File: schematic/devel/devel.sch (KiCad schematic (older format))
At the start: 65 parts, among them J1 CONN_PWR, J2 CONN_X1, J3 CONN_Y2, J4 CONN_X2, J5 CONN_Y1, Q1 Q_PMOS_GSD, Q2 Q_NMOS_GSD, U1 LM317_SOT223, U2 LM337_SOT223, U3 REF5010IDGK, U4 OPA4197

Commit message: completed pcb layout routing
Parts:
- removed C17, C18: 100u, Capacitor_SMD:CP_Elec_4x3.9, symbol Device:CP_Small
- removed D4, D5: D_Zener_Small, Diode_SMD:D_0805_2012Metric, symbol Device:D_Zener_Small
- removed D8, D9: D_Small, Diode_SMD:D_0805_2012Metric, symbol Device:D_Small
- removed Q1: Q_PMOS_GSD, Package_TO_SOT_SMD:SOT-23, symbol Device:Q_PMOS_GSD
- removed Q2: Q_NMOS_GSD, Package_TO_SOT_SMD:SOT-23, symbol Device:Q_NMOS_GSD
- removed R10, R11: 100k, Resistor_SMD:R_0805_2012Metric, symbol Device:R_Small
- removed R12, R13: 22, Resistor_SMD:R_0805_2012Metric, symbol Device:R_Small
- removed R14, R15: 100, Resistor_SMD:R_0805_2012Metric, symbol Device:R_Small
- removed TP10, TP11, TP12, TP7, TP8, TP9: TestPoint, TestPoint:TestPoint_Pad_D1.0mm, symbol Connector:TestPoint
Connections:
- wire segments 221 -> 165
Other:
- note added: "POWER CONNECTOR"
- note removed: "POWER CONNECTOR, POLARITY PROTECTION, FILTER"
- moved on the sheet: C1, C10, C11, C12, C13, C14, C15, C16, C2, C3, C4, C5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

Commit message: replaced sma connector footprint
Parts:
- J1: footprint Connector_PinHeader_1.00mm:PinHeader_1x03_P1.00mm_Vertical_SMD_Pin1Right -> Connector_PinHeader_2.54mm:PinHeader_1x03_P2.54mm_Vertical_SMD_Pin1Left
- J2, J3, J4, J5: footprint Connector_Coaxial_SMA:SMA_EdgeSlim -> Connector_Coaxial_SMA:SMA_Molex_73251-2120_EdgeMount
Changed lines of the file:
@@
 F 0 "J3" H 7250 3850 50  0000 L CNN
 F 1 "CONN_Y2" H 7100 3750 50  0000 L CNN
-F 2 "Connector_Coaxial_SMA:SMA_EdgeSlim" H 7300 3550 50  0001 C CNN
+F 2 "Connector_Coaxial_SMA:SMA_Molex_73251-2120_EdgeMount" H 7300 3550 50  0001 C CNN
 F 3 " ~" H 7300 3550 50  0001 C CNN
 	1    7300 3550
@@
 F 0 "J5" H 9150 3850 50  0000 L CNN
 F 1 "CONN_Y1" H 9000 3750 50  0000 L CNN
-F 2 "Connector_Coaxial_SMA:SMA_EdgeSlim" H 9200 3550 50  0001 C CNN
+F 2 "Connector_Coaxial_SMA:SMA_Molex_73251-2120_EdgeMount" H 9200 3550 50  0001 C CNN
 F 3 " ~" H 9200 3550 50  0001 C CNN
 	1    9200 3550
@@
 F 0 "J4" H 9150 2250 50  0000 L CNN
 F 1 "CONN_X2" H 9000 2150 50  0000 L CNN
-F 2 "Connector_Coaxial_SMA:SMA_EdgeSlim" H 9200 1950 50  0001 C CNN
+F 2 "Connector_Coaxial_SMA:SMA_Molex_73251-2120_EdgeMount" H 9200 1950 50  0001 C CNN
 F 3 " ~" H 9200 1950 50  0001 C CNN
 	1    9200 1950
@@
 F 0 "J2" H 7250 2250 50  0000 L CNN
 F 1 "CONN_X1" H 7100 2150 50  0000 L CNN
-F 2 "Connector_Coaxial_SMA:SMA_EdgeSlim" H 7300 1950 50  0001 C CNN
+F 2 "Connector_Coaxial_SMA:SMA_Molex_73251-2120_EdgeMount" H 7300 1950 50  0001 C CNN
 F 3 " ~" H 7300 1950 50  0001 C CNN
 	1    7300 1950
@@
 F 0 "J1" H 900 1800 50  0000 C CNN
 F 1 "CONN_PWR" V 750 1550 50  0000 C CNN
-F 2 "Connector_PinHeader_1.00mm:PinHeader_1x03_P1.00mm_Vertical_SMD_Pin1Right" H 850 1550 50  0001 C CNN
+F 2 "Connector_PinHeader_2.54mm:PinHeader_1x03_P2.54mm_Vertical_SMD_Pin1Left" H 850 1550 50  0001 C CNN
 F 3 "~" H 850 1550 50  0001 C CNN
 	1    850  1550

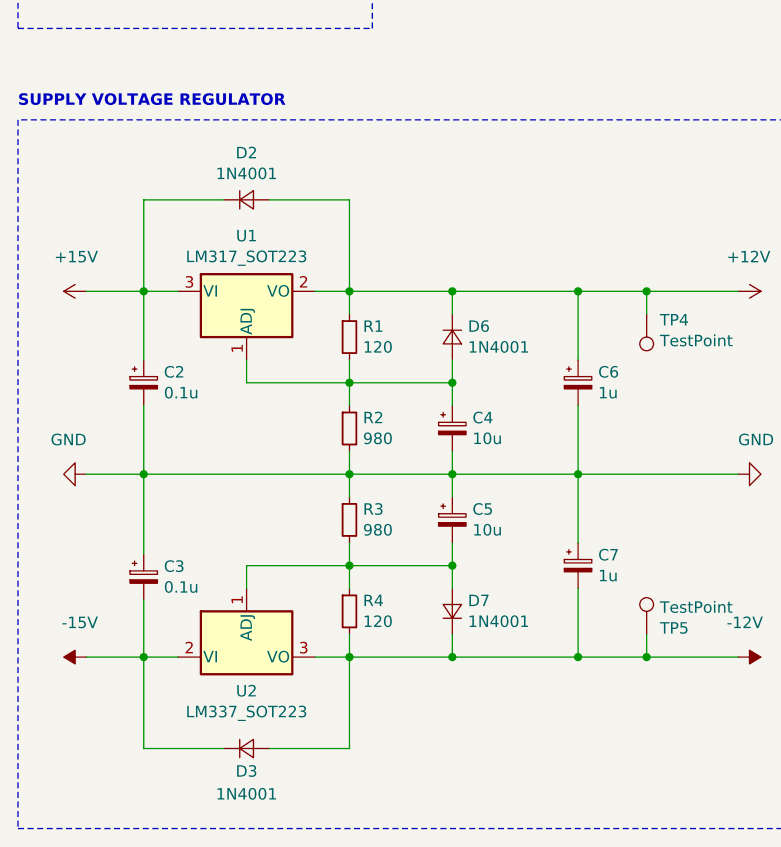
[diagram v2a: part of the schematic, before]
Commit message: updated pcb layout, added screws
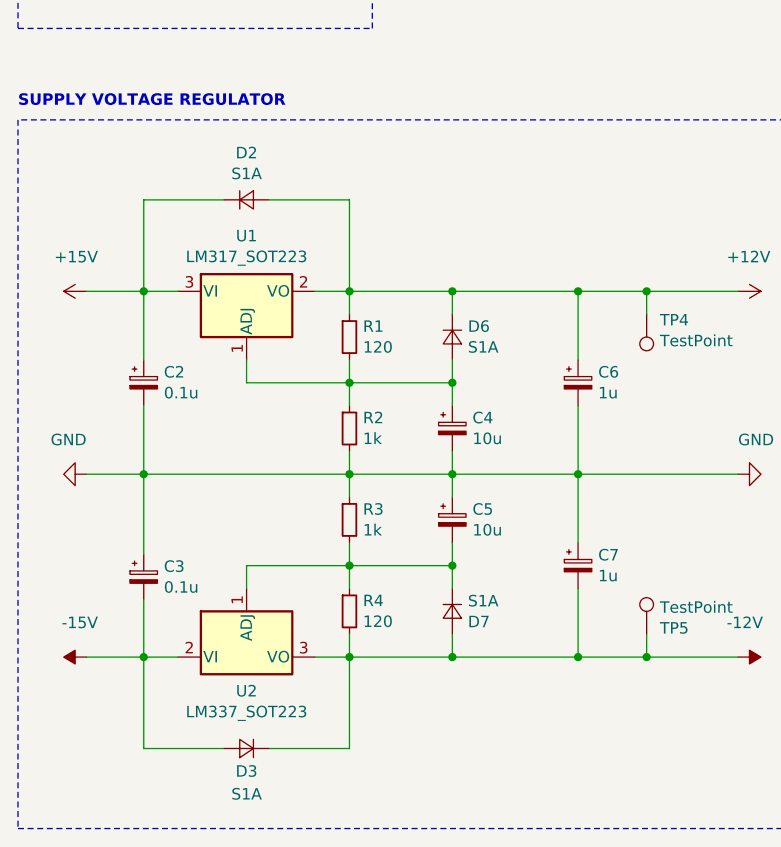
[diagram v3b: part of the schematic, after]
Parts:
- C16: footprint Capacitor_SMD:CP_Elec_4x3.9 -> Capacitor_SMD:CP_Elec_5x5.3
- C2, C3: footprint Capacitor_SMD:CP_Elec_4x3.9 -> Capacitor_SMD:CP_Elec_4x5.4
- D2, D3, D6, D7: value 1N4001 -> S1A; footprint Diode_SMD:D_0805_2012Metric -> Diode_SMD:D_SMA
- R2, R3: value 980 -> 1k
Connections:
- net -12V: now also D3.1 (K), D7.2 (A); no longer D3.2 (A), D7.1 (K)
- net -15V: now also D3.2 (A); no longer D3.1 (K)
- net at C5.2, R3.2, R4.1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: now also D7.1 (K); no longer D7.2 (A)
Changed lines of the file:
@@
 F 0 "C3" H 1288 4946 50  0000 L CNN
 F 1 "0.1u" H 1288 4855 50  0000 L CNN
-F 2 "Capacitor_SMD:CP_Elec_4x3.9" H 1200 4900 50  0001 C CNN
+F 2 "Capacitor_SMD:CP_Elec_4x5.4" H 1200 4900 50  0001 C CNN
 F 3 "~" H 1200 4900 50  0001 C CNN
 	1    1200 4900
@@
 F 0 "C2" H 1288 4096 50  0000 L CNN
 F 1 "0.1u" H 1288 4005 50  0000 L CNN
-F 2 "Capacitor_SMD:CP_Elec_4x3.9" H 1200 4050 50  0001 C CNN
+F 2 "Capacitor_SMD:CP_Elec_4x5.4" H 1200 4050 50  0001 C CNN
 F 3 "~" H 1200 4050 50  0001 C CNN
 	1    1200 4050
@@
 P 2100 4250
 F 0 "R2" H 2159 4296 50  0000 L CNN
-F 1 "980" H 2159 4205 50  0000 L CNN
+F 1 "1k" H 2159 4205 50  0000 L CNN
 F 2 "Resistor_SMD:R_0805_2012Metric" H 2100 4250 50  0001 C CNN
 F 3 "~" H 2100 4250 50  0001 C CNN
@@
 P 2100 4650
 F 0 "R3" H 2159 4696 50  0000 L CNN
-F 1 "980" H 2159 4605 50  0000 L CNN
+F 1 "1k" H 2159 4605 50  0000 L CNN
 F 2 "Resistor_SMD:R_0805_2012Metric" H 2100 4650 50  0001 C CNN
 F 3 "~" H 2100 4650 50  0001 C CNN
@@
 F 0 "C16" H 7792 5496 50  0000 L CNN
 F 1 "22u" H 7792 5405 50  0000 L CNN
-F 2 "Capacitor_SMD:CP_Elec_4x3.9" H 7700 5450 50  0001 C CNN
+F 2 "Capacitor_SMD:CP_Elec_5x5.3" H 7700 5450 50  0001 C CNN
 F 3 "~" H 7700 5450 50  0001 C CNN
 	1    7700 5450
@@
 P 1650 3250
 F 0 "D2" H 1650 3045 50  0000 C CNN
-F 1 "1N4001" H 1650 3136 50  0000 C CNN
-F 2 "Diode_SMD:D_0805_2012Metric" V 1650 3250 50  0001 C CNN
+F 1 "S1A" H 1650 3136 50  0000 C CNN
+F 2 "Diode_SMD:D_SMA" V 1650 3250 50  0001 C CNN
 F 3 "~" V 1650 3250 50  0001 C CNN
 	1    1650 3250
@@
 Wire Wire Line
 	1750 3250 2100 3250
+Wire Wire Line
+	1200 5650 1550 5650
+Wire Wire Line
+	1750 5650 2100 5650
+$Comp
+L Device:D_Small D6
+U 1 1 5D8629E9
+P 2550 3850
+F 0 "D6" V 2504 3782 50  0000 R CNN
+F 1 "S1A" V 2595 3782 50  0000 R CNN
+F 2 "Diode_SMD:D_SMA" V 2550 3850 50  0001 C CNN
+F 3 "~" V 2550 3850 50  0001 C CNN
+	1    2550 3850
+	0    -1   1    0
+$EndComp
+Wire Wire Line
+	2550 3650 2550 3750
+Wire Wire Line
+	2550 3950 2550 4050
+Wire Wire Line
+	2550 4850 2550 4950
+Wire Wire Line
+	2550 5150 2550 5250
+Wire Wire Line
+	1400 1050 1050 1050
+Connection ~ 1400 1050
+Wire Wire Line
+	1050 1550 1400 1550
+Connection ~ 1400 1550
+Wire Wire Line
+	1400 2100 1050 2100
+Connection ~ 1400 2100
+$Comp
+L Device:D_Small D7
+U 1 1 5D871F27
+P 2550 5050
+F 0 "D7" V 2596 4982 50  0000 R CNN
+F 1 "S1A" V 2505 4982 50  0000 R CNN
+F 2 "Diode_SMD:D_SMA" V 2550 5050 50  0001 C CNN
+F 3 "~" V 2550 5050 50  0001 C CNN
+	1    2550 5050
+	0    -1   1    0
+$EndComp
 $Comp
 L Device:D_Small D3
@@
 P 1650 5650
 F 0 "D3" H 1650 5550 50  0000 C CNN
-F 1 "1N4001" H 1650 5450 50  0000 C CNN
-F 2 "Diode_SMD:D_0805_2012Metric" V 1650 5650 50  0001 C CNN
+F 1 "S1A" H 1650 5450 50  0000 C CNN
+F 2 "Diode_SMD:D_SMA" V 1650 5650 50  0001 C CNN
 F 3 "~" V 1650 5650 50  0001 C CNN
 	1    1650 5650
-	1    0    0    -1
-$EndComp
-Wire Wire Line
-	1200 5650 1550 5650
-Wire Wire Line
-	1750 5650 2100 5650
-$Comp
-L Device:D_Small D6
-U 1 1 5D8629E9
-P 2550 3850
-F 0 "D6" V 2504 3782 50  0000 R CNN
-F 1 "1N4001" V 2595 3782 50  0000 R CNN
-F 2 "Diode_SMD:D_0805_2012Metric" V 2550 3850 50  0001 C CNN
-F 3 "~" V 2550 3850 50  0001 C CNN
-	1    2550 3850
-	0    -1   1    0
-$EndComp
-Wire Wire Line
-	2550 3650 2550 3750
-Wire Wire Line
-	2550 3950 2550 4050
-$Comp
-L Device:D_Small D7
-U 1 1 5D871F27
-P 2550 5050
-F 0 "D7" V 2596 4982 50  0000 R CNN
-F 1 "1N4001" V 2505 4982 50  0000 R CNN
-F 2 "Diode_SMD:D_0805_2012Metric" V 2550 5050 50  0001 C CNN
-F 3 "~" V 2550 5050 50  0001 C CNN
-	1    2550 5050
-	0    -1   -1   0
-$EndComp
-Wire Wire Line
-	2550 4850 2550 4950
-Wire Wire Line
-	2550 5150 2550 5250
-Wire Wire Line
-	1400 1050 1050 1050
-Connection ~ 1400 1050
-Wire Wire Line
-	1050 1550 1400 1550
-Connection ~ 1400 1550
-Wire Wire Line
-	1400 2100 1050 2100
-Connection ~ 1400 2100
+	-1   0    0    -1
+$EndComp
 $EndSCHEMATC

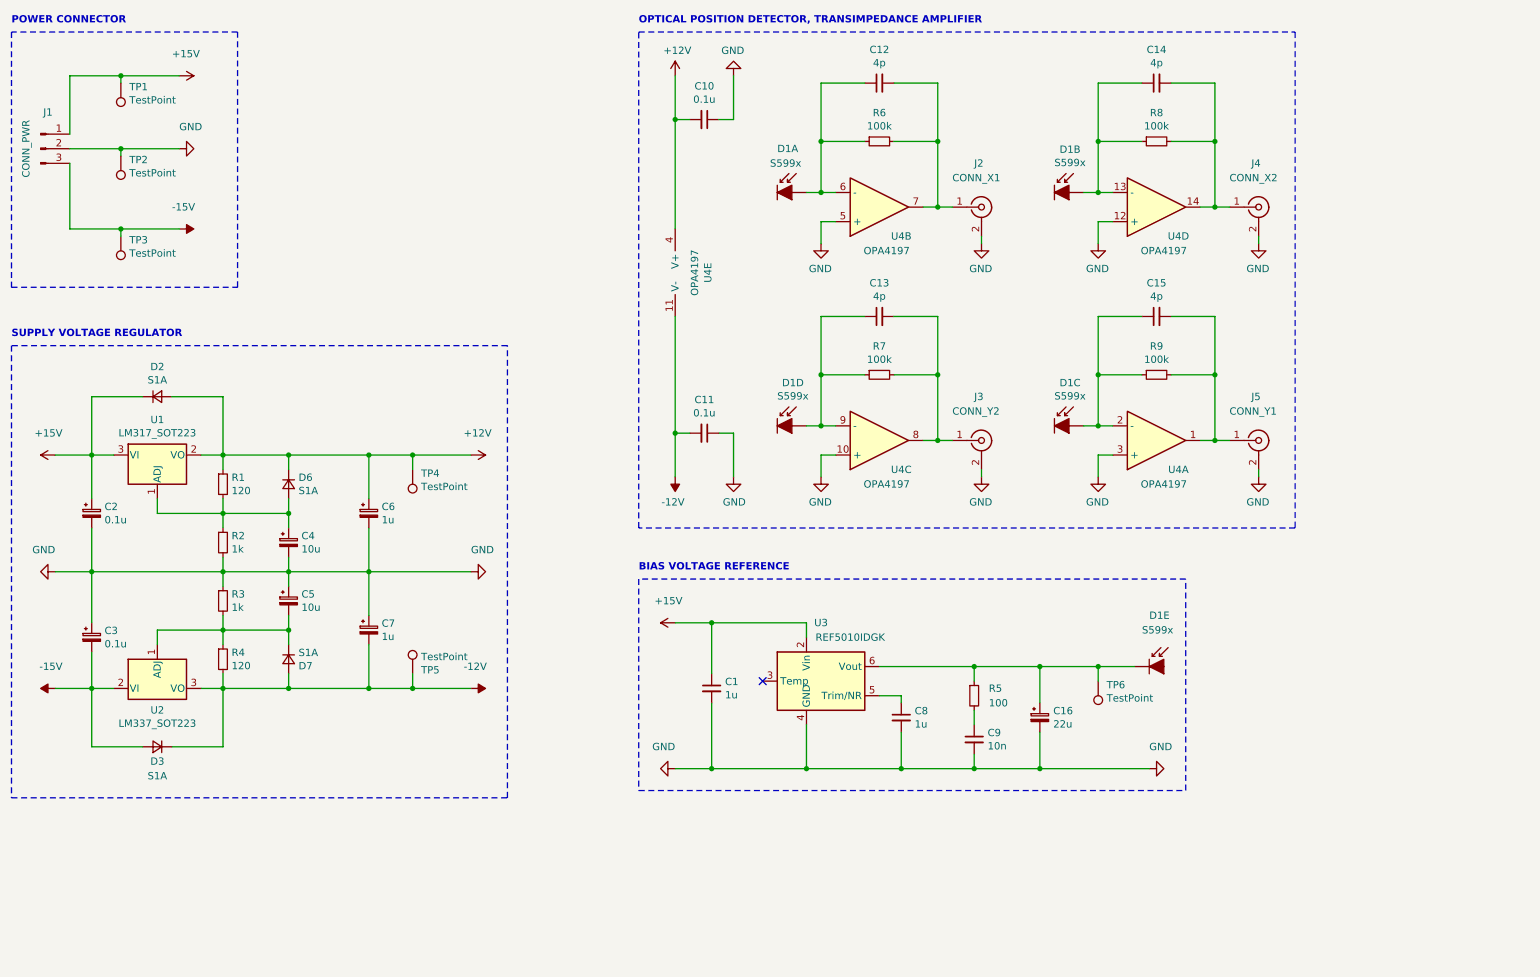
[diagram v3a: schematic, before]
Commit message: realigned vias, added silk labels
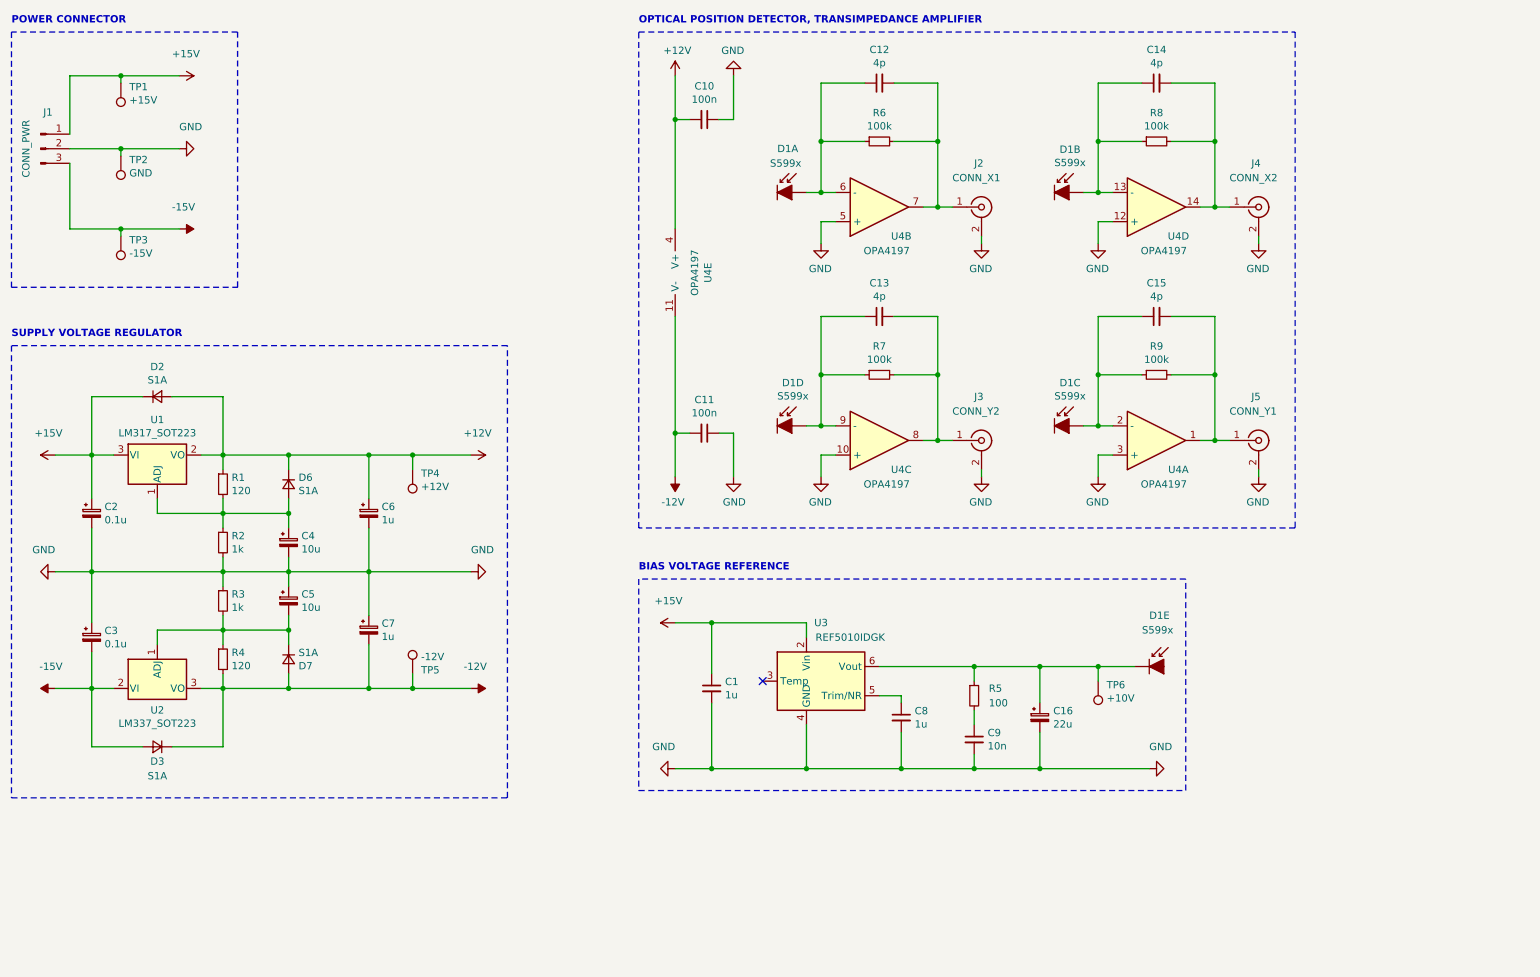
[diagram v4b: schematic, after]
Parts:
- C10, C11: value 0.1u -> 100n
- TP1: value TestPoint -> +15V
- TP2: value TestPoint -> GND
- TP3: value TestPoint -> -15V
- TP4: value TestPoint -> +12V
- TP5: value TestPoint -> -12V
- TP6: value TestPoint -> +10V
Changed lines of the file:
@@
 AR Path="/5D929D0E/5C9FE3C7" Ref="C?"  Part="1"
 F 0 "C10" V 5171 1350 50  0000 C CNN
-F 1 "0.1u" V 5262 1350 50  0000 C CNN
+F 1 "100n" V 5262 1350 50  0000 C CNN
 F 2 "Capacitor_SMD:C_0402_1005Metric" H 5400 1350 50  0001 C CNN
 F 3 "~" H 5400 1350 50  0001 C CNN
@@
 AR Path="/5D929D0E/5C9FE3D9" Ref="C?"  Part="1"
 F 0 "C11" V 5171 3500 50  0000 C CNN
-F 1 "0.1u" V 5262 3500 50  0000 C CNN
+F 1 "100n" V 5262 3500 50  0000 C CNN
 F 2 "Capacitor_SMD:C_0402_1005Metric" H 5400 3500 50  0001 C CNN
 F 3 "~" H 5400 3500 50  0001 C CNN
@@
 AR Path="/5D7CE105/5CA08158" Ref="TP?"  Part="1"
 F 0 "TP1" H 1342 1126 50  0000 R CNN
-F 1 "TestPoint" H 1342 1217 50  0000 R CNN
+F 1 "+15V" H 1342 1217 50  0000 R CNN
 F 2 "TestPoint:TestPoint_Pad_D1.0mm" H 1600 1100 50  0001 C CNN
 F 3 "~" H 1600 1100 50  0001 C CNN
@@
 AR Path="/5D7CE105/5CA08161" Ref="TP?"  Part="1"
 F 0 "TP2" H 1342 1626 50  0000 R CNN
-F 1 "TestPoint" H 1342 1717 50  0000 R CNN
+F 1 "GND" H 1342 1717 50  0000 R CNN
 F 2 "TestPoint:TestPoint_Pad_D1.0mm" H 1600 1600 50  0001 C CNN
 F 3 "~" H 1600 1600 50  0001 C CNN
@@
 AR Path="/5D7CE105/5CA0816A" Ref="TP?"  Part="1"
 F 0 "TP3" H 1342 2176 50  0000 R CNN
-F 1 "TestPoint" H 1342 2267 50  0000 R CNN
+F 1 "-15V" H 1342 2267 50  0000 R CNN
 F 2 "TestPoint:TestPoint_Pad_D1.0mm" H 1600 2150 50  0001 C CNN
 F 3 "~" H 1600 2150 50  0001 C CNN
@@
 AR Path="/5D7CE105/5CA081AC" Ref="TP?"  Part="1"
 F 0 "TP6" H 8042 5226 50  0000 R CNN
-F 1 "TestPoint" H 8042 5317 50  0000 R CNN
+F 1 "+10V" H 8042 5317 50  0000 R CNN
 F 2 "TestPoint:TestPoint_Pad_D1.0mm" H 8300 5200 50  0001 C CNN
 F 3 "~" H 8300 5200 50  0001 C CNN
@@
 AR Path="/5D7CE105/5D1A41DF" Ref="TP?"  Part="1"
 F 0 "TP4" H 3342 3776 50  0000 R CNN
-F 1 "TestPoint" H 3342 3867 50  0000 R CNN
+F 1 "+12V" H 3342 3867 50  0000 R CNN
 F 2 "TestPoint:TestPoint_Pad_D1.0mm" H 3600 3750 50  0001 C CNN
 F 3 "~" H 3600 3750 50  0001 C CNN
@@
 AR Path="/5D7CE105/5D1A4BAC" Ref="TP?"  Part="1"
 F 0 "TP5" H 3342 5176 50  0000 R CNN
-F 1 "TestPoint" H 3342 5267 50  0000 R CNN
+F 1 "-12V" H 3342 5267 50  0000 R CNN
 F 2 "TestPoint:TestPoint_Pad_D1.0mm" H 3600 5150 50  0001 C CNN
 F 3 "~" H 3600 5150 50  0001 C CNN
